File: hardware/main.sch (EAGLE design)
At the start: 100 parts, among them IC1 MPU-6050, IC2 TB6612FNG, M1 MOTOR_MOUNT_V2, M2 LED_MOUNT, M3 LED_MOUNT, M4 LED_MOUNT, M5 LED_MOUNT, M6 LED_MOUNT, M7 LED_MOUNT, Q7 IRLML2244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

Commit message: dodanie wartosci elementow
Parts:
- R1_1, R1_2, R22: value (none) -> 10k
- R25, R2_2: value (none) -> 15k
- R2_1: value (none) -> 31k
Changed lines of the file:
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@@
 <grid distance="0.1" unitdist="inch" unit="inch" style="lines" multiple="1" display="no" altdistance="0.01" altunitdist="inch" altunit="inch"/>
 <layers>
-<layer number="1" name="Top" color="4" fill="1" visible="no" active="no"/>
-<layer number="2" name="Route2" color="1" fill="3" visible="no" active="no"/>
-<layer number="3" name="Route3" color="4" fill="3" visible="no" active="no"/>
-<layer number="4" name="Route4" color="1" fill="4" visible="no" active="no"/>
-<layer number="5" name="Route5" color="4" fill="4" visible="no" active="no"/>
-<layer number="6" name="Route6" color="1" fill="8" visible="no" active="no"/>
-<layer number="7" name="Route7" color="4" fill="8" visible="no" active="no"/>
-<layer number="8" name="Route8" color="1" fill="2" visible="no" active="no"/>
-<layer number="9" name="Route9" color="4" fill="2" visible="no" active="no"/>
-<layer number="10" name="Route10" color="1" fill="7" visible="no" active="no"/>
-<layer number="11" name="Route11" color="4" fill="7" visible="no" active="no"/>
-<layer number="12" name="Route12" color="1" fill="5" visible="no" active="no"/>
-<layer number="13" name="Route13" color="4" fill="5" visible="no" active="no"/>
-<layer number="14" name="Route14" color="1" fill="6" visible="no" active="no"/>
-<layer number="15" name="Route15" color="4" fill="6" visible="no" active="no"/>
-<layer number="16" name="Bottom" color="1" fill="1" visible="no" active="no"/>
-<layer number="17" name="Pads" color="2" fill="1" visible="no" active="no"/>
-<layer number="18" name="Vias" color="2" fill="1" visible="no" active="no"/>
-<layer number="19" name="Unrouted" color="6" fill="1" visible="no" active="no"/>
-<layer number="20" name="Dimension" color="15" fill="1" visible="no" active="no"/>
-<layer number="21" name="tPlace" color="7" fill="1" visible="no" active="no"/>
-<layer number="22" name="bPlace" color="7" fill="1" visible="no" active="no"/>
-<layer number="23" name="tOrigins" color="15" fill="1" visible="no" active="no"/>
-<layer number="24" name="bOrigins" color="15" fill="1" visible="no" active="no"/>
-<layer number="25" name="tNames" color="7" fill="1" visible="no" active="no"/>
-<layer number="26" name="bNames" color="7" fill="1" visible="no" active="no"/>
-<layer number="27" name="tValues" color="7" fill="1" visible="no" active="no"/>
-<layer number="28" name="bValues" color="7" fill="1" visible="no" active="no"/>
+<layer number="1" name="Top" color="4" fill="1" visible="yes" active="no"/>
+<layer number="2" name="Route2" color="1" fill="3" visible="yes" active="no"/>
+<layer number="3" name="Route3" color="4" fill="3" visible="yes" active="no"/>
+<layer number="4" name="Route4" color="1" fill="4" visible="yes" active="no"/>
+<layer number="5" name="Route5" color="4" fill="4" visible="yes" active="no"/>
+<layer number="6" name="Route6" color="1" fill="8" visible="yes" active="no"/>
+<layer number="7" name="Route7" color="4" fill="8" visible="yes" active="no"/>
+<layer number="8" name="Route8" color="1" fill="2" visible="yes" active="no"/>
+<layer number="9" name="Route9" color="4" fill="2" visible="yes" active="no"/>
+<layer number="10" name="Route10" color="1" fill="7" visible="yes" active="no"/>
+<layer number="11" name="Route11" color="4" fill="7" visible="yes" active="no"/>
+<layer number="12" name="Route12" color="1" fill="5" visible="yes" active="no"/>
+<layer number="13" name="Route13" color="4" fill="5" visible="yes" active="no"/>
+<layer number="14" name="Route14" color="1" fill="6" visible="yes" active="no"/>
+<layer number="15" name="Route15" color="4" fill="6" visible="yes" active="no"/>
+<layer number="16" name="Bottom" color="1" fill="1" visible="yes" active="no"/>
+<layer number="17" name="Pads" color="2" fill="1" visible="yes" active="no"/>
+<layer number="18" name="Vias" color="2" fill="1" visible="yes" active="no"/>
+<layer number="19" name="Unrouted" color="6" fill="1" visible="yes" active="no"/>
+<layer number="20" name="Dimension" color="15" fill="1" visible="yes" active="no"/>
+<layer number="21" name="tPlace" color="7" fill="1" visible="yes" active="no"/>
+<layer number="22" name="bPlace" color="7" fill="1" visible="yes" active="no"/>
+<layer number="23" name="tOrigins" color="15" fill="1" visible="yes" active="no"/>
+<layer number="24" name="bOrigins" color="15" fill="1" visible="yes" active="no"/>
+<layer number="25" name="tNames" color="7" fill="1" visible="yes" active="no"/>
+<layer number="26" name="bNames" color="7" fill="1" visible="yes" active="no"/>
+<layer number="27" name="tValues" color="7" fill="1" visible="yes" active="no"/>
+<layer number="28" name="bValues" color="7" fill="1" visible="yes" active="no"/>
 <layer number="29" name="tStop" color="7" fill="3" visible="no" active="no"/>
 <layer number="30" name="bStop" color="7" fill="6" visible="no" active="no"/>
@@
 <layer number="35" name="tGlue" color="7" fill="4" visible="no" active="no"/>
 <layer number="36" name="bGlue" color="7" fill="5" visible="no" active="no"/>
-<layer number="37" name="tTest" color="7" fill="1" visible="no" active="no"/>
-<layer number="38" name="bTest" color="7" fill="1" visible="no" active="no"/>
+<layer number="37" name="tTest" color="7" fill="1" visible="yes" active="no"/>
+<layer number="38" name="bTest" color="7" fill="1" visible="yes" active="no"/>
 <layer number="39" name="tKeepout" color="4" fill="11" visible="no" active="no"/>
 <layer number="40" name="bKeepout" color="1" fill="11" visible="no" active="no"/>
@@
 <layer number="44" name="Drills" color="7" fill="1" visible="no" active="no"/>
 <layer number="45" name="Holes" color="7" fill="1" visible="no" active="no"/>
-<layer number="46" name="Milling" color="3" fill="1" visible="no" active="no"/>
-<layer number="47" name="Measures" color="7" fill="1" visible="no" active="no"/>
-<layer number="48" name="Document" color="7" fill="1" visible="no" active="no"/>
-<layer number="49" name="Reference" color="7" fill="1" visible="no" active="no"/>
-<layer number="50" name="dxf" color="7" fill="1" visible="no" active="no"/>
-<layer number="51" name="tDocu" color="7" fill="1" visible="no" active="no"/>
-<layer number="52" name="bDocu" color="7" fill="1" visible="no" active="no"/>
-<layer number="53" name="tGND_GNDA" color="7" fill="9" visible="no" active="no"/>
-<layer number="54" name="bGND_GNDA" color="1" fill="9" visible="no" active="no"/>
-<layer number="56" name="wert" color="7" fill="1" visible="no" active="no"/>
-<layer number="57" name="tCAD" color="7" fill="1" visible="no" active="no"/>
-<layer number="59" name="tCarbon" color="7" fill="1" visible="no" active="no"/>
-<layer number="60" name="bCarbon" color="7" fill="1" visible="no" active="no"/>
+<layer number="46" name="Milling" color="3" fill="1" visible="yes" active="no"/>
+<layer number="47" name="Measures" color="7" fill="1" visible="yes" active="no"/>
+<layer number="48" name="Document" color="7" fill="1" visible="yes" active="no"/>
+<layer number="49" name="Reference" color="7" fill="1" visible="yes" active="no"/>
+<layer number="50" name="dxf" color="7" fill="1" visible="yes" active="no"/>
+<layer number="51" name="tDocu" color="7" fill="1" visible="yes" active="no"/>
+<layer number="52" name="bDocu" color="7" fill="1" visible="yes" active="no"/>
+<layer number="53" name="tGND_GNDA" color="7" fill="9" visible="yes" active="no"/>
+<layer number="54" name="bGND_GNDA" color="1" fill="9" visible="yes" active="no"/>
+<layer number="56" name="wert" color="7" fill="1" visible="yes" active="no"/>
+<layer number="57" name="tCAD" color="7" fill="1" visible="yes" active="no"/>
+<layer number="59" name="tCarbon" color="7" fill="1" visible="yes" active="no"/>
+<layer number="60" name="bCarbon" color="7" fill="1" visible="yes" active="no"/>
 <layer number="90" name="Modules" color="5" fill="1" visible="yes" active="yes"/>
 <layer number="91" name="Nets" color="2" fill="1" visible="yes" active="yes"/>
@@
 <part name="Q7" library="microbuilder" deviceset="MOSFET-P" device="" value="IRLML2244"/>
 <part name="ON" library="micromouse" deviceset="PRZELACZNIK_SUWAKOWY" device=""/>
-<part name="R22" library="resistor" deviceset="R-EU_" device="R0603"/>
-<part name="R25" library="resistor" deviceset="R-EU_" device="R0603"/>
+<part name="R22" library="resistor" deviceset="R-EU_" device="R0603" value="10k"/>
+<part name="R25" library="resistor" deviceset="R-EU_" device="R0603" value="15k"/>
 <part name="SUPPLY1" library="supply2" deviceset="+7V" device="" value="+7V4"/>
 <part name="AGND30" library="supply2" deviceset="GND" device=""/>
@@
 <part name="C1_2" library="rcl" deviceset="C-EU" device="C0805" value="10u"/>
 <part name="C3_2" library="rcl" deviceset="C-EU" device="C0603" value="100n"/>
-<part name="R1_2" library="rcl" deviceset="R-EU_" device="R0603"/>
-<part name="R2_2" library="rcl" deviceset="R-EU_" device="R0603"/>
+<part name="R1_2" library="rcl" deviceset="R-EU_" device="R0603" value="10k"/>
+<part name="R2_2" library="rcl" deviceset="R-EU_" device="R0603" value="15k"/>
 <part name="C2_2" library="rcl" deviceset="C-EU" device="C0805" value="10u"/>
 <part name="U1" library="micromouse" deviceset="ST1S40" device=""/>
 <part name="C1_1" library="rcl" deviceset="C-EU" device="C0805" value="10u"/>
 <part name="C3_1" library="rcl" deviceset="C-EU" device="C0603" value="100n"/>
-<part name="R1_1" library="rcl" deviceset="R-EU_" device="R0603"/>
-<part name="R2_1" library="rcl" deviceset="R-EU_" device="R0603"/>
+<part name="R1_1" library="rcl" deviceset="R-EU_" device="R0603" value="10k"/>
+<part name="R2_1" library="rcl" deviceset="R-EU_" device="R0603" value="31k"/>
 <part name="C2_1" library="rcl" deviceset="C-EU" device="C0805" value="10u"/>
 <part name="AGND31" library="supply2" deviceset="GND" device=""/>

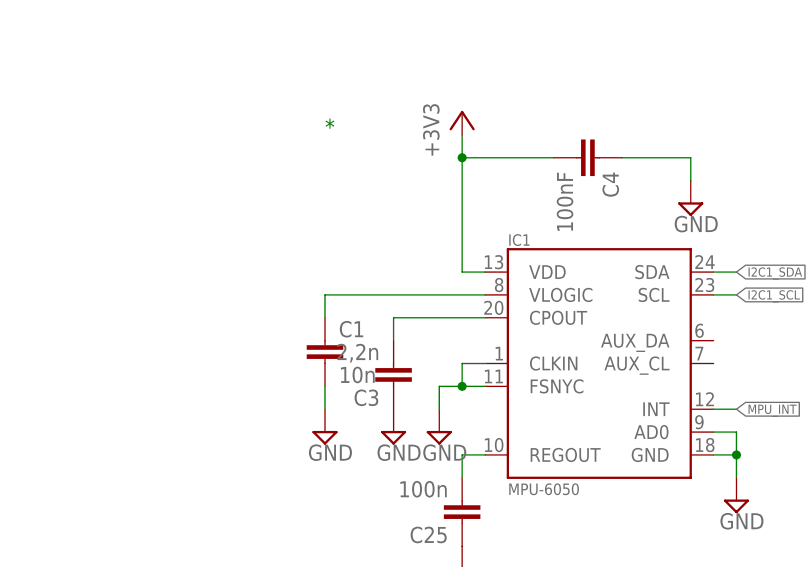
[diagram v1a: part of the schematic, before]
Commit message: gyro vlogic fixed
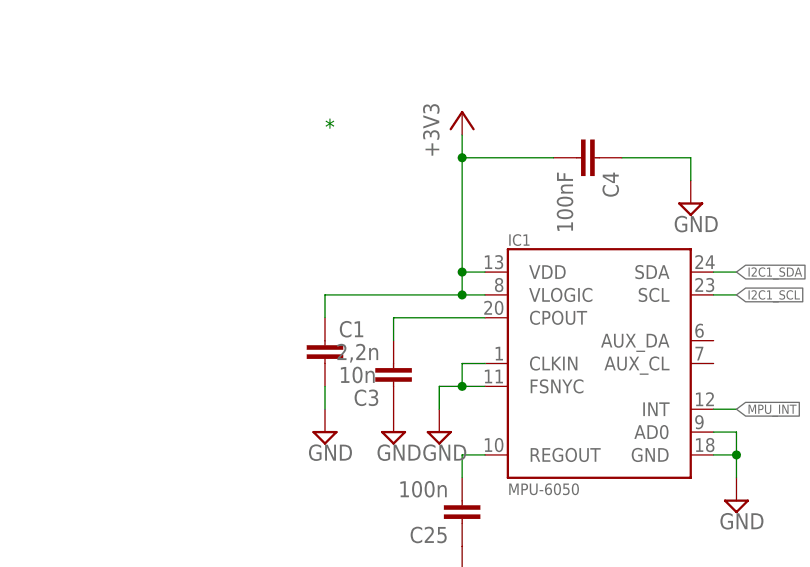
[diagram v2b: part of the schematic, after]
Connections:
- removed net N$34: C1.1, IC1.VLOGIC
- net +3V3: now also C1.1, IC1.VLOGIC
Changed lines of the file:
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@@
 <grid distance="0.1" unitdist="inch" unit="inch" style="lines" multiple="1" display="no" altdistance="0.01" altunitdist="inch" altunit="inch"/>
 <layers>
-<layer number="1" name="Top" color="4" fill="1" visible="yes" active="no"/>
-<layer number="2" name="Route2" color="1" fill="3" visible="yes" active="no"/>
-<layer number="3" name="Route3" color="4" fill="3" visible="yes" active="no"/>
-<layer number="4" name="Route4" color="1" fill="4" visible="yes" active="no"/>
-<layer number="5" name="Route5" color="4" fill="4" visible="yes" active="no"/>
-<layer number="6" name="Route6" color="1" fill="8" visible="yes" active="no"/>
-<layer number="7" name="Route7" color="4" fill="8" visible="yes" active="no"/>
-<layer number="8" name="Route8" color="1" fill="2" visible="yes" active="no"/>
-<layer number="9" name="Route9" color="4" fill="2" visible="yes" active="no"/>
-<layer number="10" name="Route10" color="1" fill="7" visible="yes" active="no"/>
-<layer number="11" name="Route11" color="4" fill="7" visible="yes" active="no"/>
-<layer number="12" name="Route12" color="1" fill="5" visible="yes" active="no"/>
-<layer number="13" name="Route13" color="4" fill="5" visible="yes" active="no"/>
-<layer number="14" name="Route14" color="1" fill="6" visible="yes" active="no"/>
-<layer number="15" name="Route15" color="4" fill="6" visible="yes" active="no"/>
-<layer number="16" name="Bottom" color="1" fill="1" visible="yes" active="no"/>
-<layer number="17" name="Pads" color="2" fill="1" visible="yes" active="no"/>
-<layer number="18" name="Vias" color="2" fill="1" visible="yes" active="no"/>
-<layer number="19" name="Unrouted" color="6" fill="1" visible="yes" active="no"/>
-<layer number="20" name="Dimension" color="15" fill="1" visible="yes" active="no"/>
-<layer number="21" name="tPlace" color="7" fill="1" visible="yes" active="no"/>
-<layer number="22" name="bPlace" color="7" fill="1" visible="yes" active="no"/>
-<layer number="23" name="tOrigins" color="15" fill="1" visible="yes" active="no"/>
-<layer number="24" name="bOrigins" color="15" fill="1" visible="yes" active="no"/>
-<layer number="25" name="tNames" color="7" fill="1" visible="yes" active="no"/>
-<layer number="26" name="bNames" color="7" fill="1" visible="yes" active="no"/>
-<layer number="27" name="tValues" color="7" fill="1" visible="yes" active="no"/>
-<layer number="28" name="bValues" color="7" fill="1" visible="yes" active="no"/>
+<layer number="1" name="Top" color="4" fill="1" visible="no" active="no"/>
+<layer number="2" name="Route2" color="1" fill="3" visible="no" active="no"/>
+<layer number="3" name="Route3" color="4" fill="3" visible="no" active="no"/>
+<layer number="4" name="Route4" color="1" fill="4" visible="no" active="no"/>
+<layer number="5" name="Route5" color="4" fill="4" visible="no" active="no"/>
+<layer number="6" name="Route6" color="1" fill="8" visible="no" active="no"/>
+<layer number="7" name="Route7" color="4" fill="8" visible="no" active="no"/>
+<layer number="8" name="Route8" color="1" fill="2" visible="no" active="no"/>
+<layer number="9" name="Route9" color="4" fill="2" visible="no" active="no"/>
+<layer number="10" name="Route10" color="1" fill="7" visible="no" active="no"/>
+<layer number="11" name="Route11" color="4" fill="7" visible="no" active="no"/>
+<layer number="12" name="Route12" color="1" fill="5" visible="no" active="no"/>
+<layer number="13" name="Route13" color="4" fill="5" visible="no" active="no"/>
+<layer number="14" name="Route14" color="1" fill="6" visible="no" active="no"/>
+<layer number="15" name="Route15" color="4" fill="6" visible="no" active="no"/>
+<layer number="16" name="Bottom" color="1" fill="1" visible="no" active="no"/>
+<layer number="17" name="Pads" color="2" fill="1" visible="no" active="no"/>
+<layer number="18" name="Vias" color="2" fill="1" visible="no" active="no"/>
+<layer number="19" name="Unrouted" color="6" fill="1" visible="no" active="no"/>
+<layer number="20" name="Dimension" color="15" fill="1" visible="no" active="no"/>
+<layer number="21" name="tPlace" color="7" fill="1" visible="no" active="no"/>
+<layer number="22" name="bPlace" color="7" fill="1" visible="no" active="no"/>
+<layer number="23" name="tOrigins" color="15" fill="1" visible="no" active="no"/>
+<layer number="24" name="bOrigins" color="15" fill="1" visible="no" active="no"/>
+<layer number="25" name="tNames" color="7" fill="1" visible="no" active="no"/>
+<layer number="26" name="bNames" color="7" fill="1" visible="no" active="no"/>
+<layer number="27" name="tValues" color="7" fill="1" visible="no" active="no"/>
+<layer number="28" name="bValues" color="7" fill="1" visible="no" active="no"/>
 <layer number="29" name="tStop" color="7" fill="3" visible="no" active="no"/>
 <layer number="30" name="bStop" color="7" fill="6" visible="no" active="no"/>
@@
 <layer number="35" name="tGlue" color="7" fill="4" visible="no" active="no"/>
 <layer number="36" name="bGlue" color="7" fill="5" visible="no" active="no"/>
-<layer number="37" name="tTest" color="7" fill="1" visible="yes" active="no"/>
-<layer number="38" name="bTest" color="7" fill="1" visible="yes" active="no"/>
+<layer number="37" name="tTest" color="7" fill="1" visible="no" active="no"/>
+<layer number="38" name="bTest" color="7" fill="1" visible="no" active="no"/>
 <layer number="39" name="tKeepout" color="4" fill="11" visible="no" active="no"/>
 <layer number="40" name="bKeepout" color="1" fill="11" visible="no" active="no"/>
@@
 <layer number="44" name="Drills" color="7" fill="1" visible="no" active="no"/>
 <layer number="45" name="Holes" color="7" fill="1" visible="no" active="no"/>
-<layer number="46" name="Milling" color="3" fill="1" visible="yes" active="no"/>
-<layer number="47" name="Measures" color="7" fill="1" visible="yes" active="no"/>
-<layer number="48" name="Document" color="7" fill="1" visible="yes" active="no"/>
-<layer number="49" name="Reference" color="7" fill="1" visible="yes" active="no"/>
-<layer number="50" name="dxf" color="7" fill="1" visible="yes" active="no"/>
-<layer number="51" name="tDocu" color="7" fill="1" visible="yes" active="no"/>
-<layer number="52" name="bDocu" color="7" fill="1" visible="yes" active="no"/>
-<layer number="53" name="tGND_GNDA" color="7" fill="9" visible="yes" active="no"/>
-<layer number="54" name="bGND_GNDA" color="1" fill="9" visible="yes" active="no"/>
-<layer number="56" name="wert" color="7" fill="1" visible="yes" active="no"/>
-<layer number="57" name="tCAD" color="7" fill="1" visible="yes" active="no"/>
-<layer number="59" name="tCarbon" color="7" fill="1" visible="yes" active="no"/>
-<layer number="60" name="bCarbon" color="7" fill="1" visible="yes" active="no"/>
+<layer number="46" name="Milling" color="3" fill="1" visible="no" active="no"/>
+<layer number="47" name="Measures" color="7" fill="1" visible="no" active="no"/>
+<layer number="48" name="Document" color="7" fill="1" visible="no" active="no"/>
+<layer number="49" name="Reference" color="7" fill="1" visible="no" active="no"/>
+<layer number="50" name="dxf" color="7" fill="1" visible="no" active="no"/>
+<layer number="51" name="tDocu" color="7" fill="1" visible="no" active="no"/>
+<layer number="52" name="bDocu" color="7" fill="1" visible="no" active="no"/>
+<layer number="53" name="tGND_GNDA" color="7" fill="9" visible="no" active="no"/>
+<layer number="54" name="bGND_GNDA" color="1" fill="9" visible="no" active="no"/>
+<layer number="56" name="wert" color="7" fill="1" visible="no" active="no"/>
+<layer number="57" name="tCAD" color="7" fill="1" visible="no" active="no"/>
+<layer number="59" name="tCarbon" color="7" fill="1" visible="no" active="no"/>
+<layer number="60" name="bCarbon" color="7" fill="1" visible="no" active="no"/>
 <layer number="90" name="Modules" color="5" fill="1" visible="yes" active="yes"/>
 <layer number="91" name="Nets" color="2" fill="1" visible="yes" active="yes"/>
@@
 <wire x1="-93.98" y1="246.38" x2="-93.98" y2="248.92" width="0.1524" layer="91"/>
 <junction x="-93.98" y="246.38"/>
+<pinref part="IC1" gate="G$1" pin="VLOGIC"/>
+<pinref part="C1" gate="G$1" pin="1"/>
+<wire x1="-91.44" y1="231.14" x2="-93.98" y2="231.14" width="0.1524" layer="91"/>
+<wire x1="-93.98" y1="231.14" x2="-109.22" y2="231.14" width="0.1524" layer="91"/>
+<wire x1="-109.22" y1="231.14" x2="-109.22" y2="228.6" width="0.1524" layer="91"/>
+<wire x1="-93.98" y1="233.68" x2="-93.98" y2="231.14" width="0.1524" layer="91"/>
+<junction x="-93.98" y="233.68"/>
+<junction x="-93.98" y="231.14"/>
 </segment>
 <segment>
@@
 </segment>
 </net>
-<net name="N$34" class="0">
-<segment>
-<pinref part="IC1" gate="G$1" pin="VLOGIC"/>
-<pinref part="C1" gate="G$1" pin="1"/>
-<wire x1="-91.44" y1="231.14" x2="-109.22" y2="231.14" width="0.1524" layer="91"/>
-<wire x1="-109.22" y1="231.14" x2="-109.22" y2="228.6" width="0.1524" layer="91"/>
-</segment>
-</net>
